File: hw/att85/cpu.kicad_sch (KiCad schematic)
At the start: 20 parts, among them J201 Conn_01x06, J202 Conn_01x04, J203 Conn_01x03, U201 STM32G030K8Tx, U202 74AHCT125, U203 CAT24C256

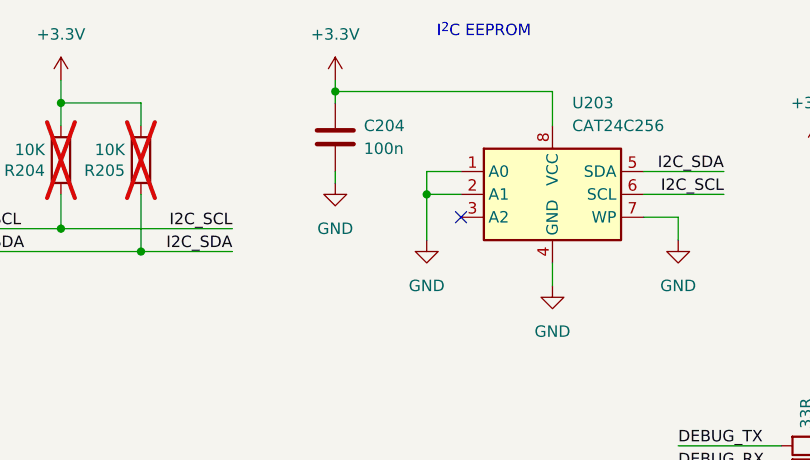
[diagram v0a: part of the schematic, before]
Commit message: chore(hw): move debug UART header
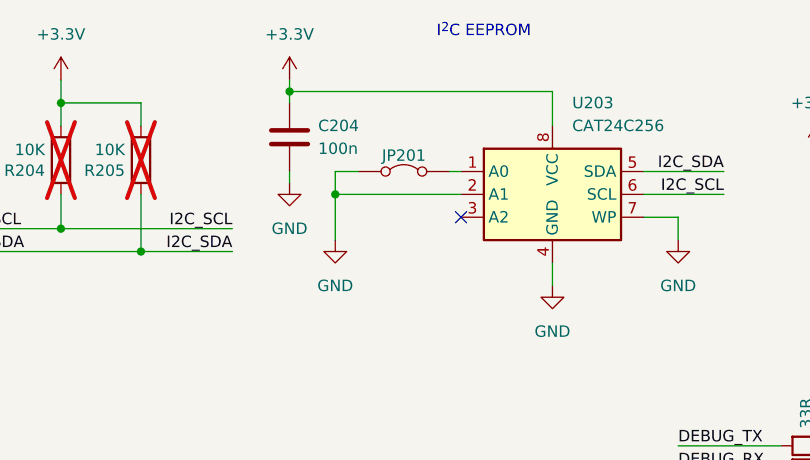
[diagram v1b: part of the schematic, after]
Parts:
- added JP201: Jumper_2_Bridged, Jumper:SolderJumper-2_P1.3mm_Bridged_RoundedPad1.0x1.5mm, symbol Jumper:Jumper_2_Bridged
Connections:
- net GND: now also JP201.1 (A); no longer U203.1 (A0)
- new net: JP201.2 (B), U203.1 (A0)
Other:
- moved on the sheet: C204
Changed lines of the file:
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@@
 	)
 	(junction
-		(at 195.58 25.4)
+		(at 190.5 25.4)
 		(diameter 0)
 		(color 0 0 0 0)
 	)
 	(junction
-		(at 205.74 36.83)
+		(at 195.58 36.83)
 		(diameter 0)
 		(color 0 0 0 0)
@@
 	(wire
 		(pts
-			(xy 195.58 26.67) (xy 195.58 25.4)
+			(xy 190.5 26.67) (xy 190.5 25.4)
 		)
 		(stroke
@@
 	(wire
 		(pts
-			(xy 195.58 25.4) (xy 219.71 25.4)
+			(xy 190.5 25.4) (xy 219.71 25.4)
 		)
 		(stroke
@@
 	(wire
 		(pts
-			(xy 195.58 35.56) (xy 195.58 34.29)
+			(xy 190.5 35.56) (xy 190.5 34.29)
 		)
 		(stroke
@@
 	(wire
 		(pts
-			(xy 106.68 86.36) (xy 121.92 86.36)
+			(xy 208.28 34.29) (xy 209.55 34.29)
 		)
 		(stroke
@@
 	(wire
 		(pts
-			(xy 27.94 26.67) (xy 27.94 27.94)
+			(xy 106.68 86.36) (xy 121.92 86.36)
 		)
 		(stroke
@@
 	(wire
 		(pts
-			(xy 205.74 34.29) (xy 209.55 34.29)
+			(xy 27.94 26.67) (xy 27.94 27.94)
 		)
 		(stroke
@@
 	(wire
 		(pts
-			(xy 205.74 41.91) (xy 205.74 36.83)
+			(xy 195.58 41.91) (xy 195.58 36.83)
 		)
 		(stroke
@@
 	(wire
 		(pts
-			(xy 205.74 36.83) (xy 205.74 34.29)
+			(xy 195.58 36.83) (xy 195.58 34.29)
 		)
 		(stroke
@@
 	(wire
 		(pts
-			(xy 195.58 25.4) (xy 195.58 24.13)
+			(xy 190.5 25.4) (xy 190.5 24.13)
+		)
+		(stroke
+			(width 0)
+			(type default)
+		)
+	)
+	(wire
+		(pts
+			(xy 195.58 34.29) (xy 198.12 34.29)
 		)
 		(stroke
@@
 	(wire
 		(pts
-			(xy 205.74 36.83) (xy 209.55 36.83)
+			(xy 195.58 36.83) (xy 209.55 36.83)
 		)
 		(stroke
@@
 	)
 	(symbol
+		(lib_id "Jumper:Jumper_2_Bridged")
+		(at 203.2 34.29 0)
+		(unit 1)
+		(exclude_from_sim yes)
+		(in_bom yes)
+		(on_board yes)
+		(dnp no)
+		(property "Reference" "JP201"
+			(at 203.2 32.512 0)
+			(effects
+				(font
+					(size 1.27 1.27)
+				)
+			)
+		)
+		(property "Value" "Jumper_2_Bridged"
+			(at 203.2 31.75 0)
+			(effects
+				(font
+					(size 1.27 1.27)
+				)
+				(hide yes)
+			)
+		)
+		(property "Footprint" "Jumper:SolderJumper-2_P1.3mm_Bridged_RoundedPad1.0x1.5mm"
+			(at 203.2 34.29 0)
+			(effects
+				(font
+					(size 1.27 1.27)
+				)
+				(hide yes)
+			)
+		)
+		(property "Datasheet" "~"
+			(at 203.2 34.29 0)
+			(effects
+				(font
+					(size 1.27 1.27)
+				)
+				(hide yes)
+			)
+		)
+		(property "Description" "Jumper, 2-pole, closed/bridged"
+			(at 203.2 34.29 0)
+			(effects
+				(font
+					(size 1.27 1.27)
+				)
+				(hide yes)
+			)
+		)
+		(pin "2"
+		)
+		(pin "1"
+		)
+		(instances
+			(project ""
+				(path "/fc4ba96f-a9f8-4f1a-a9c5-2b16679a6770/32819f2b-3e26-4dff-931e-dc604d389a45"
+					(reference "JP201")
+					(unit 1)
+				)
+			)
+		)
+	)
+	(symbol
 		(lib_id "power:GND")
 		(at 85.09 55.88 0)
@@
 	(symbol
 		(lib_id "power:GND")
-		(at 195.58 35.56 0)
+		(at 190.5 35.56 0)
 		(unit 1)
 		(exclude_from_sim no)
@@
 		(fields_autoplaced yes)
 		(property "Reference" "#PWR0214"
-			(at 195.58 41.91 0)
+			(at 190.5 41.91 0)
 			(effects
 				(font
@@
 		)
 		(property "Value" "GND"
-			(at 195.58 40.64 0)
+			(at 190.5 40.64 0)
 			(effects
 				(font
@@
 		)
 		(property "Footprint" ""
-			(at 195.58 35.56 0)
+			(at 190.5 35.56 0)
 			(effects
 				(font
@@
 		)
 		(property "Datasheet" ""
-			(at 195.58 35.56 0)
+			(at 190.5 35.56 0)
 			(effects
 				(font
@@
 		)
 		(property "Description" "Power symbol creates a global label with name \"GND\" , ground"
-			(at 195.58 35.56 0)
+			(at 190.5 35.56 0)
 			(effects
 				(font
@@
 	(symbol
 		(lib_id "power:+3.3V")
-		(at 195.58 24.13 0)
+		(at 190.5 24.13 0)
 		(unit 1)
 		(exclude_from_sim no)
@@
 		(fields_autoplaced yes)
 		(property "Reference" "#PWR0213"
-			(at 195.58 27.94 0)
+			(at 190.5 27.94 0)
 			(effects
 				(font
@@
 		)
 		(property "Value" "+3.3V"
-			(at 195.58 19.05 0)
+			(at 190.5 19.05 0)
 			(effects
 				(font
@@
 		)
 		(property "Footprint" ""
-			(at 195.58 24.13 0)
+			(at 190.5 24.13 0)
 			(effects
 				(font
@@
 		)
 		(property "Datasheet" ""
-			(at 195.58 24.13 0)
+			(at 190.5 24.13 0)
 			(effects
 				(font
@@
 		)
 		(property "Description" "Power symbol creates a global label with name \"+3.3V\""
-			(at 195.58 24.13 0)
+			(at 190.5 24.13 0)
 			(effects
 				(font
@@
 	(symbol
 		(lib_id "power:GND")
-		(at 205.74 41.91 0)
+		(at 195.58 41.91 0)
 		(unit 1)
 		(exclude_from_sim no)
@@
 		(fields_autoplaced yes)
 		(property "Reference" "#PWR0216"
-			(at 205.74 48.26 0)
+			(at 195.58 48.26 0)
 			(effects
 				(font
@@
 		)
 		(property "Value" "GND"
-			(at 205.74 46.99 0)
+			(at 195.58 46.99 0)
 			(effects
 				(font
@@
 		)
 		(property "Footprint" ""
-			(at 205.74 41.91 0)
+			(at 195.58 41.91 0)
 			(effects
 				(font
@@
 		)
 		(property "Datasheet" ""
-			(at 205.74 41.91 0)
+			(at 195.58 41.91 0)
 			(effects
 				(font
@@
 		)
 		(property "Description" "Power symbol creates a global label with name \"GND\" , ground"
-			(at 205.74 41.91 0)
+			(at 195.58 41.91 0)
 			(effects
 				(font
@@
 	(symbol
 		(lib_id "Device:C")
-		(at 195.58 30.48 0)
+		(at 190.5 30.48 0)
 		(unit 1)
 		(exclude_from_sim no)
@@
 		(fields_autoplaced yes)
 		(property "Reference" "C204"
-			(at 198.755 29.21 0)
+			(at 193.675 29.21 0)
 			(effects
 				(font
@@
 		)
 		(property "Value" "100n"
-			(at 198.755 31.75 0)
+			(at 193.675 31.75 0)
 			(effects
 				(font
@@
 		)
 		(property "Footprint" "Capacitor_SMD:C_0805_2012Metric_Pad1.18x1.45mm_HandSolder"
-			(at 196.5452 34.29 0)
+			(at 191.4652 34.29 0)
 			(effects
 				(font
@@
 		)
 		(property "Datasheet" "~"
-			(at 195.58 30.48 0)
+			(at 190.5 30.48 0)
 			(effects
 				(font
@@
 		)
 		(property "Description" "Unpolarized capacitor"
-			(at 195.58 30.48 0)
+			(at 190.5 30.48 0)
 			(effects
 				(font

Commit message: chore(hw): almost final layout
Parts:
- removed JP201: Jumper_2_Bridged, Jumper:SolderJumper-2_P1.3mm_Bridged_RoundedPad1.0x1.5mm, symbol Jumper:Jumper_2_Bridged
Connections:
- net +3.3V: now also J201.4 (Pin_4); no longer J201.1 (Pin_1)
- net GND: now also J201.2 (Pin_2), U203.1 (A0); no longer J201.4 (Pin_4)
- net SWCLK: now also J201.1 (Pin_1); no longer J201.3 (Pin_3)
- net SWDIO: now also J201.3 (Pin_3); no longer J201.2 (Pin_2)
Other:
- note added: "Debug UART"
- note added: "LED Chain Data Driver"
- moved on the sheet: C201, C202, C203, C204, D201, D202, D203, J201, J203, R201, R202, R203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
